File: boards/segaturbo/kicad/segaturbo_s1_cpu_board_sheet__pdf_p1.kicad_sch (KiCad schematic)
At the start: 69 parts, among them IC104 74LS138, IC106 74LS245, IC107a 74LS08, IC107b 74LS08, IC107c 74LS08, IC108a 74LS74, IC108b 74LS74, IC109 74LS08, IC115 74S161, IC116 74S161, IC118 74LS20, IC119 74LS109, IC11a 74LS20, IC120a 74S74, IC120b 74S74, IC124 74LS138, IC128c 74LS14, IC128d 74LS14, IC128e 74LS14, IC128f 74LS14, IC129 74LS123, IC130a 74S04, IC130b 74S04, IC130c 74S04, IC130d 74S04, IC62 UPB425, IC63 74LS174, IC64a 74LS109, IC64b 74LS109, IC65 74S161, IC66 74S161, IC69 74LS04, IC77a 74LS139, IC78 74LS244, IC79 74LS244, IC7a 74LS04, IC90 PAL16L8, IC91 Z80, IC92a 74LS32, IC92c 74LS32, IC92d 74LS32, IC93a 74LS74, IC93b 74LS74, IC94a 74LS86, IC94c 74LS86, IC94d 74LS86, X1 19.968MHz

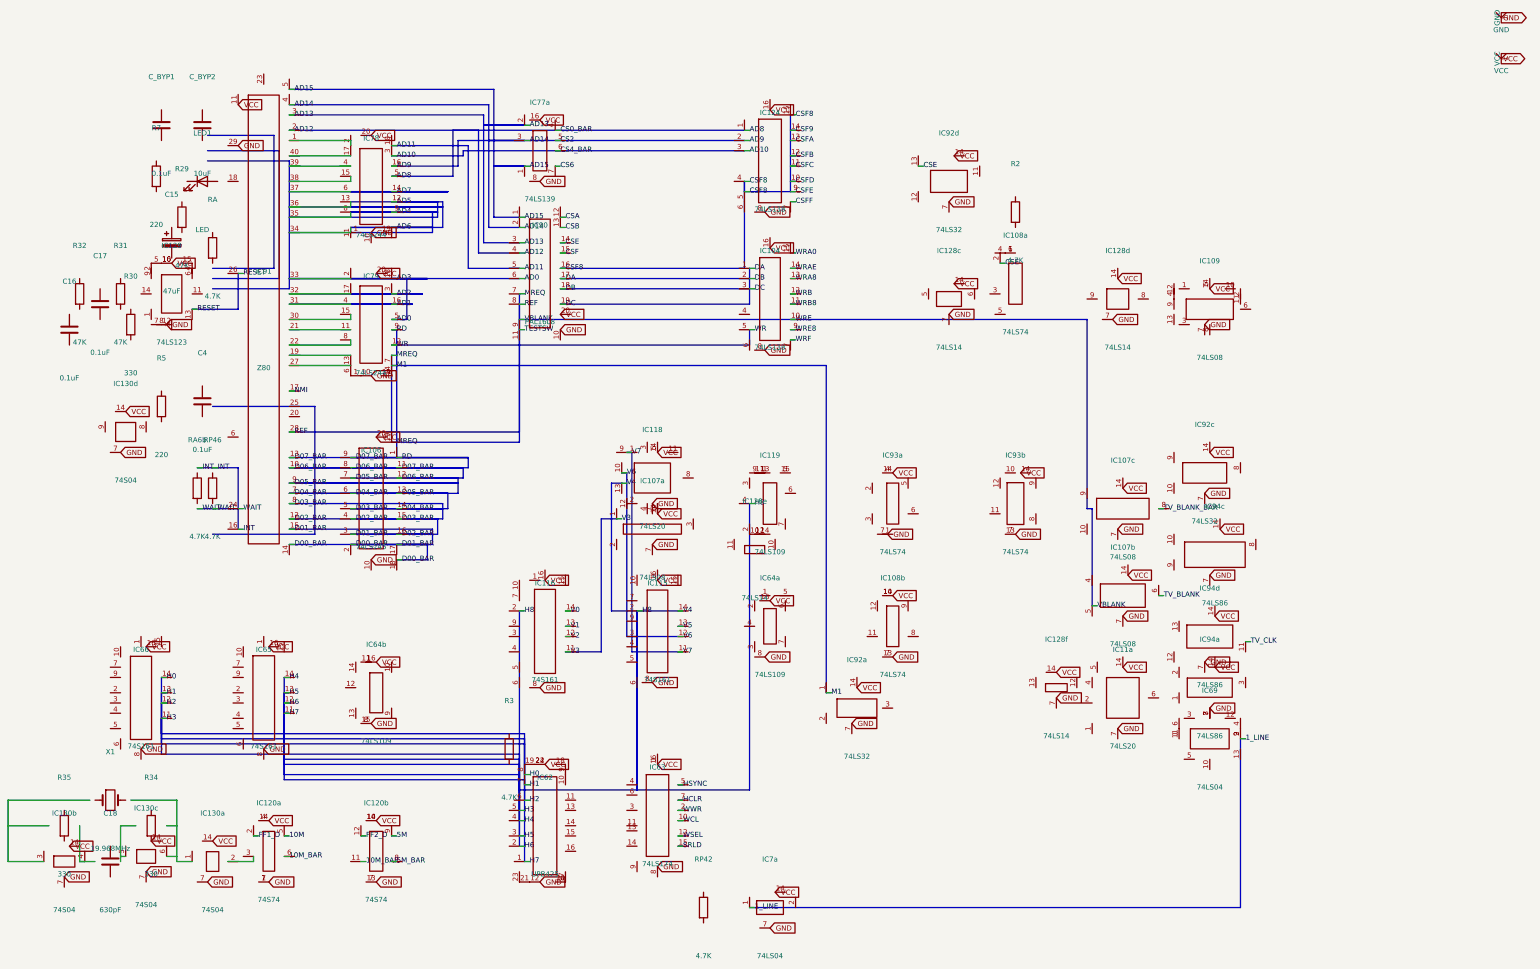
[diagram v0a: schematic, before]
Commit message: Fix KiCad pin-aligned generated symbols
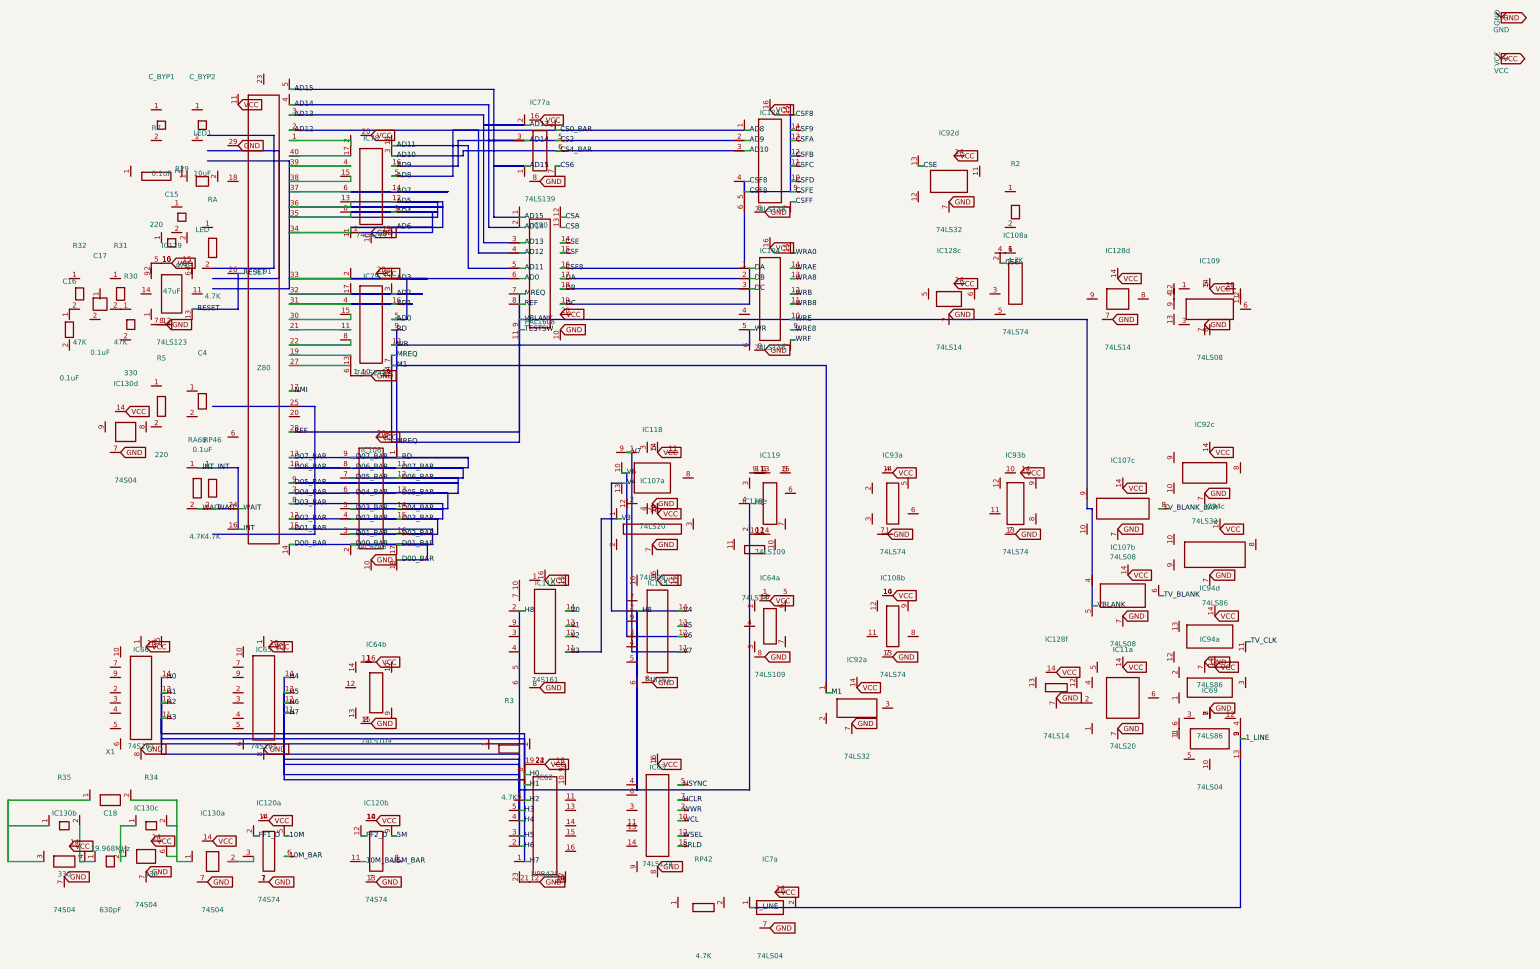
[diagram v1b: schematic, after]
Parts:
- C15: symbol Device:C_Polarized -> user:_chip_C15
- C16: symbol Device:C -> user:_chip_C16
- C17: symbol Device:C -> user:_chip_C17
- C18: symbol Device:C -> user:_chip_C18
- C4: symbol Device:C -> user:_chip_C4
- C_BYP1: symbol Device:C -> user:_chip_C_BYP1
- C_BYP2: symbol Device:C -> user:_chip_C_BYP2
- LED1: symbol Device:LED -> user:_chip_LED1
- R2: symbol Device:R -> user:_chip_R2
- R29: symbol Device:R -> user:_chip_R29
- R3: symbol Device:R -> user:_chip_R3
- R30: symbol Device:R -> user:_chip_R30
- R31: symbol Device:R -> user:_chip_R31
- R32: symbol Device:R -> user:_chip_R32
- R34: symbol Device:R -> user:_chip_R34
- R35: symbol Device:R -> user:_chip_R35
- R5: symbol Device:R -> user:_chip_R5
- R7: symbol Device:R -> user:_chip_R7
- RA: symbol Device:R -> user:_chip_RA
- RA6b: symbol Device:R -> user:_chip_RA6b
- RP42: symbol Device:R -> user:_chip_RP42
- RP46: symbol Device:R -> user:_chip_RP46
- X1: symbol Device:Crystal -> user:_chip_X1
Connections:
- net INT: now also RA6b.1, RP46.1
- net VCC: no longer R34.2
- net WAIT: now also RA6b.2, RP46.2
- net at IC130c.5 (3A): now also C18.2, R34.1
- net at IC130a.1 (1A), IC130c.6 (3Y): now also R34.2, X1.2
- net at X1.1: now also IC130b.3 (2A), R35.1
- net at R35.2: now also C18.1, IC130b.4 (2Y)
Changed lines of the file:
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@@
   )
   (symbol
-    (lib_id "Device:Crystal")
+    (lib_id "user:_chip_X1")
     (at 54.61 212.09 0)
     (unit 1)
@@
   )
   (symbol
-    (lib_id "Device:R")
+    (lib_id "user:_chip_R34")
     (at 64.77 218.44 0)
     (unit 1)
@@
   )
   (symbol
-    (lib_id "Device:R")
+    (lib_id "user:_chip_R35")
     (at 43.18 218.44 0)
     (unit 1)
@@
   )
   (symbol
-    (lib_id "Device:C")
+    (lib_id "user:_chip_C18")
     (at 54.61 227.33 0)
     (unit 1)
@@
   )
   (symbol
-    (lib_id "Device:R")
+    (lib_id "user:_chip_R2")
     (at 279.4 66.04 0)
     (unit 1)
@@
   )
   (symbol
-    (lib_id "Device:R")
+    (lib_id "user:_chip_R7")
     (at 66.04 57.15 0)
     (unit 1)
@@
   )
   (symbol
-    (lib_id "Device:R")
+    (lib_id "user:_chip_RP46")
     (at 80.01 134.62 0)
     (unit 1)
@@
   )
   (symbol
-    (lib_id "Device:R")
+    (lib_id "user:_chip_RP42")
     (at 201.93 238.76 0)
     (unit 1)
@@
   )
   (symbol
-    (lib_id "Device:C")
+    (lib_id "user:_chip_C_BYP1")
     (at 67.31 44.45 0)
     (unit 1)
@@
   )
   (symbol
-    (lib_id "Device:C")
+    (lib_id "user:_chip_C_BYP2")
     (at 77.47 44.45 0)
     (unit 1)
@@
   )
   (symbol
-    (lib_id "Device:LED")
+    (lib_id "user:_chip_LED1")
     (at 77.47 58.42 0)
     (unit 1)
@@
   )
   (symbol
-    (lib_id "Device:R")
+    (lib_id "user:_chip_R29")
     (at 72.39 67.31 0)
     (unit 1)
@@
   )
   (symbol
-    (lib_id "Device:R")
+    (lib_id "user:_chip_RA")
     (at 80.01 74.93 0)
     (unit 1)
@@
   )
   (symbol
-    (lib_id "Device:C_Polarized")
+    (lib_id "user:_chip_C15")
     (at 69.85 73.66 0)
     (unit 1)
@@
   )
   (symbol
-    (lib_id "Device:R")
+    (lib_id "user:_chip_R32")
     (at 46.99 86.36 0)
     (unit 1)
@@
   )
   (symbol
-    (lib_id "Device:R")
+    (lib_id "user:_chip_R31")
     (at 57.15 86.36 0)
     (unit 1)
@@
   )
   (symbol
-    (lib_id "Device:R")
+    (lib_id "user:_chip_R30")
     (at 59.69 93.98 0)
     (unit 1)
@@
   )
   (symbol
-    (lib_id "Device:C")
+    (lib_id "user:_chip_C17")
     (at 52.07 88.9 0)
     (unit 1)
@@
   )
   (symbol
-    (lib_id "Device:R")
+    (lib_id "user:_chip_R5")
     (at 67.31 114.3 0)
     (unit 1)
@@
   )
   (symbol
-    (lib_id "Device:C")
+    (lib_id "user:_chip_C4")
     (at 77.47 113.03 0)
     (unit 1)
@@
   )
   (symbol
-    (lib_id "Device:R")
+    (lib_id "user:_chip_RA6b")
     (at 76.2 134.62 0)
     (unit 1)
@@
   )
   (symbol
-    (lib_id "Device:C")
+    (lib_id "user:_chip_C16")
     (at 44.45 95.25 0)
     (unit 1)
@@
   )
   (symbol
-    (lib_id "Device:R")
+    (lib_id "user:_chip_R3")
     (at 153.67 199.39 0)
     (unit 1)
